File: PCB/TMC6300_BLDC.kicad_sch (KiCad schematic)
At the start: 1 part, among them U4 TMC6300-LA-T_C5274455

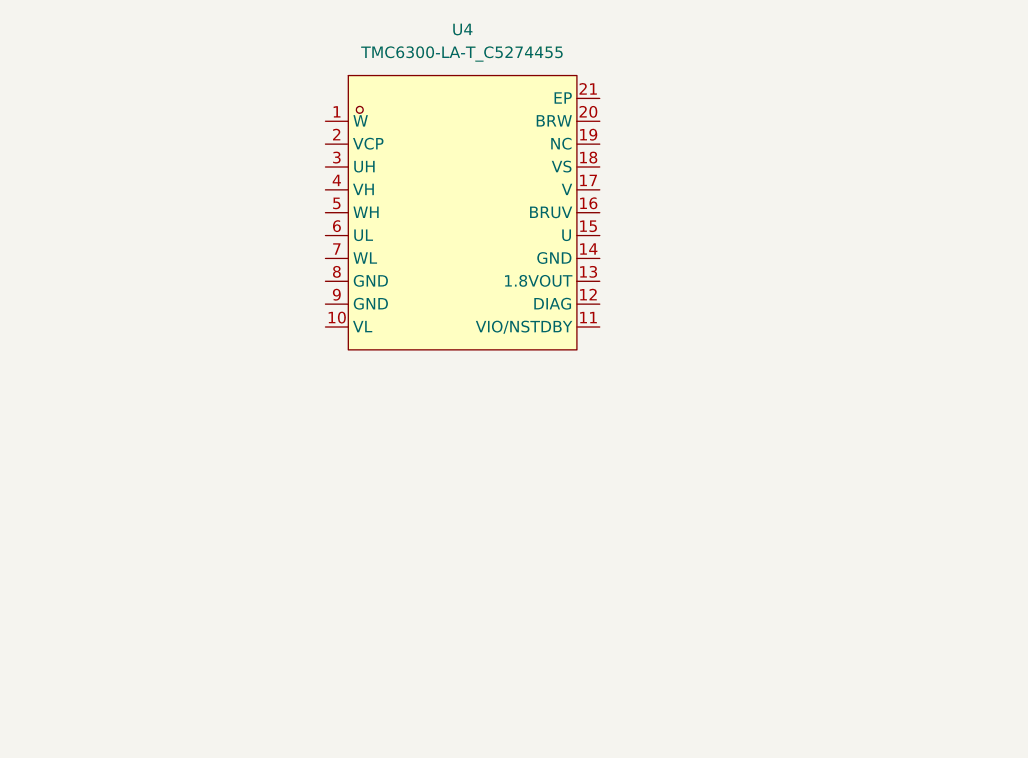
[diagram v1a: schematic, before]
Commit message: Added bldc driver
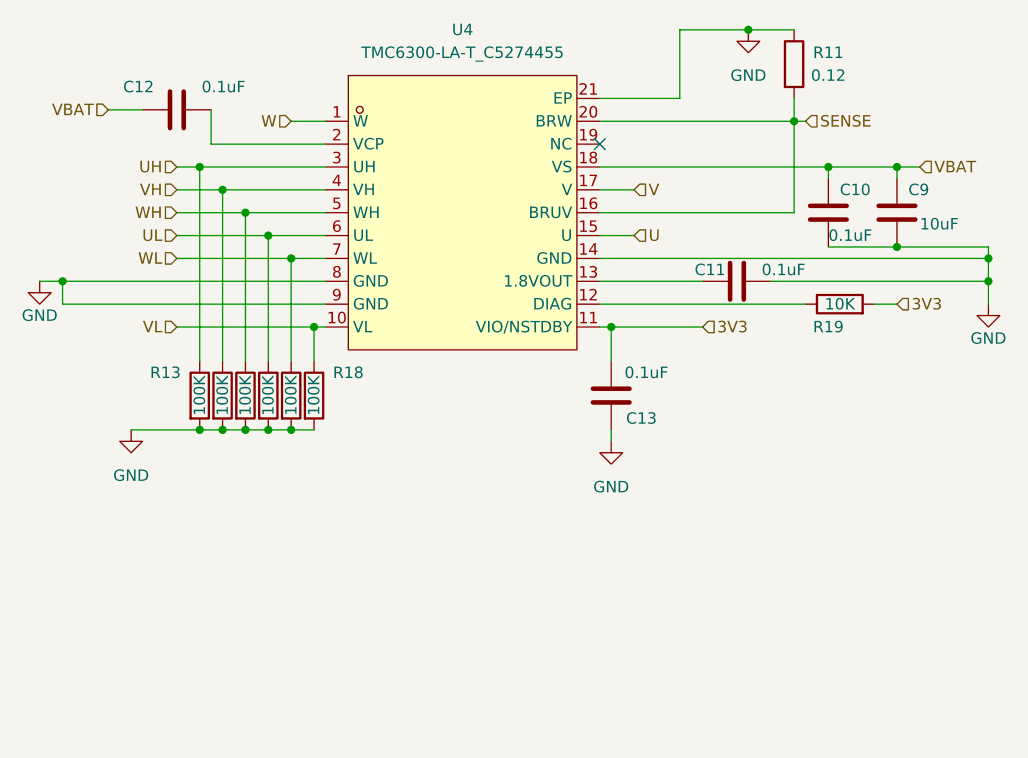
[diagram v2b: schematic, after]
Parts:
- added C10, C11, C12, C13: 0.1uF, Capacitor_SMD:C_0402_1005Metric, symbol Device:C
- added C9: 10uF, Capacitor_SMD:C_0402_1005Metric, symbol Device:C
- added R11: 0.12, Resistor_SMD:R_0402_1005Metric_Pad0.72x0.64mm_HandSolder, symbol Device:R
- added R13, R14, R15, R16, R17, R18: 100K, Resistor_SMD:R_0402_1005Metric_Pad0.72x0.64mm_HandSolder, symbol Device:R
- added R19: 10K, Resistor_SMD:R_0402_1005Metric_Pad0.72x0.64mm_HandSolder, symbol Device:R
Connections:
- net W: now reaches U4.1 (W)
- net VL: now reaches U4.10 (VL)
- net VL: now also R18.1
- net 3V3: now reaches U4.11 (VIO/NSTDBY)
- net 3V3: now also C13.2, R19.2
- net at U4.12 (DIAG): now also R19.1
- net at U4.13 (1.8VOUT): now also C11.1
- net GND: now reaches U4.14 (GND)
- net GND: now also U4.21 (EP), U4.8 (GND), U4.9 (GND), C10.2, C11.2, C13.1, C9.2, R11.1, R13.2, R14.2, R15.2, R16.2, R17.2, R18.2
- net U: now reaches U4.15 (U)
- net SENSE: now reaches U4.16 (BRUV)
- net SENSE: now also U4.20 (BRW), R11.2
- net V: now reaches U4.17 (V)
- net VBAT: now reaches U4.18 (VS)
- net VBAT: now also C10.1, C12.1, C9.1
- net at U4.2 (VCP): now also C12.2
- net UH: now reaches U4.3 (UH)
- net UH: now also R13.1
- net VH: now reaches U4.4 (VH)
- net VH: now also R14.1
- net WH: now reaches U4.5 (WH)
- net WH: now also R15.1
- net UL: now reaches U4.6 (UL)
- net UL: now also R16.1
- net WL: now reaches U4.7 (WL)
- net WL: now also R17.1
- no-connect marks 0 -> 1

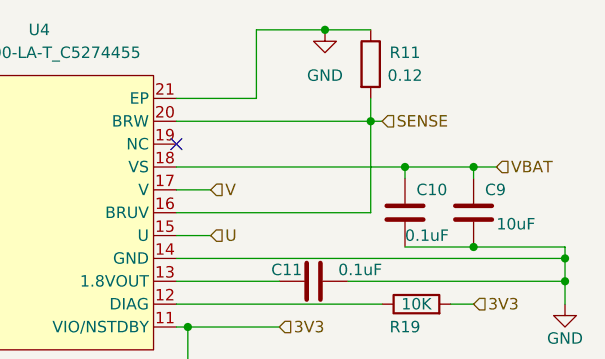
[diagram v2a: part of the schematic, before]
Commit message: BLDC driver done
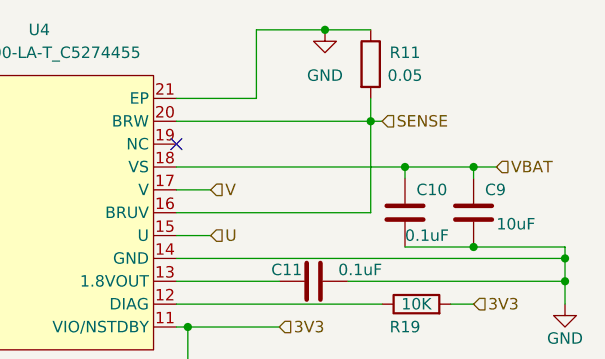
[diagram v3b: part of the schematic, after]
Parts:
- R11: value 0.12 -> 0.05; footprint Resistor_SMD:R_0402_1005Metric_Pad0.72x0.64mm_HandSolder -> Resistor_SMD:R_2010_5025Metric_Pad1.40x2.65mm_HandSolder
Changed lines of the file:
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@@
 			)
 		)
-		(property "Value" "0.12"
+		(property "Value" "0.05"
 			(at 173.99 87.63 0)
 			(effects
@@
 			)
 		)
-		(property "Footprint" "Resistor_SMD:R_0402_1005Metric_Pad0.72x0.64mm_HandSolder"
+		(property "Footprint" "Resistor_SMD:R_2010_5025Metric_Pad1.40x2.65mm_HandSolder"
 			(at 168.402 86.36 90)
 			(effects

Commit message: Finished schematic
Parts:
- C10, C12: value 0.1uF -> 0.1uF 10V
- C13: value 0.1uF -> 0.1uF 6.3V
- C9: value 10uF -> 10uF 10V
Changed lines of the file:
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@@
 			)
 		)
-		(property "Value" "0.1uF"
-			(at 156.21 120.65 0)
+		(property "Value" "0.1uF 6.3V"
+			(at 154.432 120.65 0)
 			(effects
 				(font
@@
 		(dnp no)
 		(property "Reference" "C12"
-			(at 99.06 88.9 90)
+			(at 100.076 89.916 90)
 			(effects
 				(font
@@
 			)
 		)
-		(property "Value" "0.1uF"
-			(at 109.22 88.9 90)
+		(property "Value" "0.1uF 10V"
+			(at 103.632 94.996 90)
 			(effects
 				(font
@@
 			)
 		)
-		(property "Value" "10uF"
-			(at 184.15 104.14 0)
+		(property "Value" "10uF 10V"
+			(at 182.372 105.41 0)
 			(effects
 				(font
@@
 			)
 		)
-		(property "Value" "0.1uF"
-			(at 173.99 105.41 0)
-			(effects
-				(font
+		(property "Value" "0.1uF 10V"
+			(at 168.402 105.41 0)
+			(effects
+				(font

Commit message: PCB layout done
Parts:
- removed R11: 0.05, Resistor_SMD:R_2010_5025Metric_Pad1.40x2.65mm_HandSolder, symbol Device:R
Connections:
- net SENSE is gone; now on net GND: U4.16 (BRUV), U4.20 (BRW)
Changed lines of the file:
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@@
-	)
-	(junction
-		(at 170.18 92.71)
-		(diameter 0)
-		(color 0 0 0 0)
-	)
-	(junction
-		(at 165.1 82.55)
-		(diameter 0)
-		(color 0 0 0 0)
 	)
 	(junction
@@
 	)
 	(junction
+		(at 153.67 90.17)
+		(diameter 0)
+		(color 0 0 0 0)
+	)
+	(junction
 		(at 191.77 110.49)
 		(diameter 0)
@@
 	(wire
 		(pts
+			(xy 153.67 92.71) (xy 153.67 90.17)
+		)
+		(stroke
+			(width 0)
+			(type default)
+		)
+	)
+	(wire
+		(pts
 			(xy 181.61 97.79) (xy 184.15 97.79)
 		)
@@
 	(wire
 		(pts
-			(xy 148.59 90.17) (xy 157.48 90.17)
+			(xy 148.59 90.17) (xy 153.67 90.17)
 		)
 		(stroke
@@
 	(wire
 		(pts
+			(xy 153.67 90.17) (xy 163.83 90.17)
+		)
+		(stroke
+			(width 0)
+			(type default)
+		)
+	)
+	(wire
+		(pts
 			(xy 116.84 115.57) (xy 116.84 119.38)
 		)
@@
 	(wire
 		(pts
-			(xy 157.48 90.17) (xy 157.48 82.55)
-		)
-		(stroke
-			(width 0)
-			(type default)
-		)
-	)
-	(wire
-		(pts
 			(xy 106.68 100.33) (xy 118.11 100.33)
 		)
@@
 	(wire
 		(pts
-			(xy 148.59 102.87) (xy 170.18 102.87)
-		)
-		(stroke
-			(width 0)
-			(type default)
-		)
-	)
-	(wire
-		(pts
 			(xy 109.22 127) (xy 111.76 127)
 		)
@@
 	(wire
 		(pts
-			(xy 170.18 90.17) (xy 170.18 92.71)
-		)
-		(stroke
-			(width 0)
-			(type default)
-		)
-	)
-	(wire
-		(pts
 			(xy 149.86 115.57) (xy 149.86 119.38)
 		)
@@
 	(wire
 		(pts
-			(xy 170.18 102.87) (xy 170.18 92.71)
-		)
-		(stroke
-			(width 0)
-			(type default)
-		)
-	)
-	(wire
-		(pts
 			(xy 101.6 102.87) (xy 109.22 102.87)
 		)
@@
 	(wire
 		(pts
-			(xy 165.1 82.55) (xy 170.18 82.55)
-		)
-		(stroke
-			(width 0)
-			(type default)
-		)
-	)
-	(wire
-		(pts
 			(xy 191.77 107.95) (xy 191.77 110.49)
 		)
@@
 	(wire
 		(pts
+			(xy 148.59 92.71) (xy 153.67 92.71)
+		)
+		(stroke
+			(width 0)
+			(type default)
+		)
+	)
+	(wire
+		(pts
 			(xy 111.76 105.41) (xy 118.11 105.41)
 		)
@@
 	(wire
 		(pts
-			(xy 148.59 92.71) (xy 170.18 92.71)
+			(xy 148.59 102.87) (xy 158.75 102.87)
 		)
 		(stroke
@@
 	(wire
 		(pts
-			(xy 157.48 82.55) (xy 165.1 82.55)
-		)
-		(stroke
-			(width 0)
-			(type default)
-		)
-	)
-	(wire
-		(pts
 			(xy 148.59 97.79) (xy 173.99 97.79)
 		)
@@
 		(pts
 			(xy 101.6 105.41) (xy 111.76 105.41)
-		)
-		(stroke
-			(width 0)
-			(type default)
-		)
-	)
-	(wire
-		(pts
-			(xy 170.18 92.71) (xy 171.45 92.71)
 		)
 		(stroke
@@
 			)
 			(justify right)
-		)
-	)
-	(hierarchical_label "SENSE"
-		(shape input)
-		(at 171.45 92.71 0)
-		(effects
-			(font
-				(size 1.27 1.27)
-			)
-			(justify left)
 		)
 	)
@@
 	)
 	(symbol
+		(lib_id "power:GND")
+		(at 163.83 90.17 0)
+		(unit 1)
+		(exclude_from_sim no)
+		(in_bom yes)
+		(on_board yes)
+		(dnp no)
+		(fields_autoplaced yes)
+		(property "Reference" "#PWR059"
+			(at 163.83 96.52 0)
+			(effects
+				(font
+					(size 1.27 1.27)
+				)
+				(hide yes)
+			)
+		)
+		(property "Value" "GND"
+			(at 163.83 95.25 0)
+			(effects
+				(font
+					(size 1.27 1.27)
+				)
+			)
+		)
+		(property "Footprint" ""
+			(at 163.83 90.17 0)
+			(effects
+				(font
+					(size 1.27 1.27)
+				)
+				(hide yes)
+			)
+		)
+		(property "Datasheet" ""
+			(at 163.83 90.17 0)
+			(effects
+				(font
+					(size 1.27 1.27)
+				)
+				(hide yes)
+			)
+		)
+		(property "Description" "Power symbol creates a global label with name \"GND\" , ground"
+			(at 163.83 90.17 0)
+			(effects
+				(font
+					(size 1.27 1.27)
+				)
+				(hide yes)
+			)
+		)
+		(pin "1"
+		)
+		(instances
+			(project ""
+				(path "/64c66767-4367-4391-b4db-5d3ae338f23b/f7d2473e-319a-4a76-8dbf-73a91e1f555e"
+					(reference "#PWR059")
+					(unit 1)
+				)
+			)
+		)
+	)
+	(symbol
 		(lib_id "Device:R")
 		(at 114.3 123.19 0)
@@
 				(path "/64c66767-4367-4391-b4db-5d3ae338f23b/f7d2473e-319a-4a76-8dbf-73a91e1f555e"
 					(reference "R13")
-					(unit 1)
-				)
-			)
-		)
-	)
-	(symbol
-		(lib_id "power:GND")
-		(at 165.1 82.55 0)
-		(unit 1)
-		(exclude_from_sim no)
-		(in_bom yes)
-		(on_board yes)
-		(dnp no)
-		(fields_autoplaced yes)
-		(property "Reference" "#PWR018"
-			(at 165.1 88.9 0)
-			(effects
-				(font
-					(size 1.27 1.27)
-				)
-				(hide yes)
-			)
-		)
-		(property "Value" "GND"
-			(at 165.1 87.63 0)
-			(effects
-				(font
-					(size 1.27 1.27)
-				)
-			)
-		)
-		(property "Footprint" ""
-			(at 165.1 82.55 0)
-			(effects
-				(font
-					(size 1.27 1.27)
-				)
-				(hide yes)
-			)
-		)
-		(property "Datasheet" ""
-			(at 165.1 82.55 0)
-			(effects
-				(font
-					(size 1.27 1.27)
-				)
-				(hide yes)
-			)
-		)
-		(property "Description" "Power symbol creates a global label with name \"GND\" , ground"
-			(at 165.1 82.55 0)
-			(effects
-				(font
-					(size 1.27 1.27)
-				)
-				(hide yes)
-			)
-		)
-		(pin "1"
-		)
-		(instances
-			(project ""
-				(path "/64c66767-4367-4391-b4db-5d3ae338f23b/f7d2473e-319a-4a76-8dbf-73a91e1f555e"
-					(reference "#PWR018")
 					(unit 1)
 				)
@@
 	(symbol
 		(lib_id "Device:R")
-		(at 170.18 86.36 0)
-		(unit 1)
-		(exclude_from_sim no)
-		(in_bom yes)
-		(on_board yes)
-		(dnp no)
-		(property "Reference" "R11"
-			(at 173.99 85.09 0)
-			(effects
-				(font
-					(size 1.27 1.27)
-				)
-			)
-		)
-		(property "Value" "0.05"
-			(at 173.99 87.63 0)
-			(effects
-				(font
-					(size 1.27 1.27)
-				)
-			)
-		)
-		(property "Footprint" "Resistor_SMD:R_2010_5025Metric_Pad1.40x2.65mm_HandSolder"
-			(at 168.402 86.36 90)
-			(effects
-				(font
-					(size 1.27 1.27)
-				)
-				(hide yes)
-			)
-		)
-		(property "Datasheet" "~"
-			(at 170.18 86.36 0)
-			(effects
-				(font
-					(size 1.27 1.27)
-				)
-				(hide yes)
-			)
-		)
-		(property "Description" "Resistor"
-			(at 170.18 86.36 0)
-			(effects
-				(font
-					(size 1.27 1.27)
-				)
-				(hide yes)
-			)
-		)
-		(pin "1"
-		)
-		(pin "2"
-		)
-		(instances
-			(project "detentOne"
-				(path "/64c66767-4367-4391-b4db-5d3ae338f23b/f7d2473e-319a-4a76-8dbf-73a91e1f555e"
-					(reference "R11")
-					(unit 1)
-				)
-			)
-		)
-	)
-	(symbol
-		(lib_id "Device:R")
 		(at 116.84 123.19 0)
 		(unit 1)
@@
 					(unit 1)
 				)
+			)
+		)
+	)
+	(symbol
+		(lib_id "power:GND")
+		(at 158.75 102.87 0)
+		(unit 1)
+		(exclude_from_sim no)
+		(in_bom yes)
+		(on_board yes)
+		(dnp no)
+		(property "Reference" "#PWR018"
+			(at 158.75 109.22 0)
+			(effects
+				(font
+					(size 1.27 1.27)
+				)
+				(hide yes)
+			)
+		)
+		(property "Value" "GND"
+			(at 161.036 106.172 0)
+			(effects
+				(font
+					(size 1.27 1.27)
+				)
+			)
+		)
+		(property "Footprint" ""
+			(at 158.75 102.87 0)
+			(effects
+				(font
+					(size 1.27 1.27)
+				)
+				(hide yes)
+			)
+		)
+		(property "Datasheet" ""
+			(at 158.75 102.87 0)
+			(effects
+				(font
+					(size 1.27 1.27)
+				)
+				(hide yes)
+			)
+		)
+		(property "Description" "Power symbol creates a global label with name \"GND\" , ground"
+			(at 158.75 102.87 0)
+			(effects
+				(font
+					(size 1.27 1.27)
+				)
+				(hide yes)
+			)
+		)
+		(pin "1"
+		)
+		(instances
+			(project "detentOne"
+				(path "/64c66767-4367-4391-b4db-5d3ae338f23b/f7d2473e-319a-4a76-8dbf-73a91e1f555e"
+					(reference "#PWR018")
+					(unit 1)
+				)

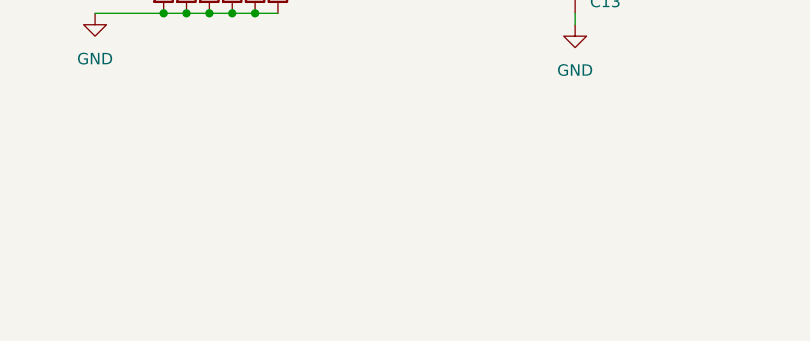
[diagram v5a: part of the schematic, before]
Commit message: removed lipo circuitry
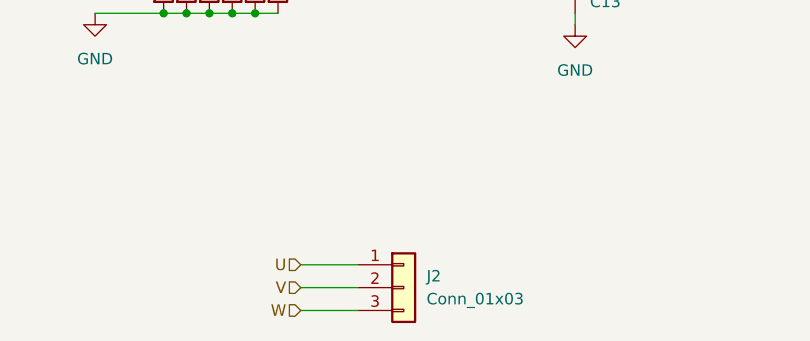
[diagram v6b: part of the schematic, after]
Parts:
- added J2: Conn_01x03, Connector_PinHeader_2.54mm:PinHeader_1x03_P2.54mm_Horizontal, symbol Connector_Generic:Conn_01x03
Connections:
- net U: now also J2.1 (Pin_1)
- net V: now also J2.2 (Pin_2)
- net W: now also J2.3 (Pin_3)
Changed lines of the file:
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@@
+	(wire
+		(pts
+			(xy 119.38 154.94) (xy 125.73 154.94)
+		)
+		(stroke
+			(width 0)
+			(type default)
+		)
+	)
 	(wire
 		(pts
@@
 	(wire
 		(pts
+			(xy 119.38 160.02) (xy 125.73 160.02)
+		)
+		(stroke
+			(width 0)
+			(type default)
+		)
+	)
+	(wire
+		(pts
 			(xy 109.22 102.87) (xy 118.11 102.87)
 		)
@@
 		(pts
 			(xy 173.99 97.79) (xy 181.61 97.79)
+		)
+		(stroke
+			(width 0)
+			(type default)
+		)
+	)
+	(wire
+		(pts
+			(xy 119.38 157.48) (xy 125.73 157.48)
 		)
 		(stroke
@@
 		)
 	)
+	(hierarchical_label "V"
+		(shape input)
+		(at 119.38 157.48 180)
+		(effects
+			(font
+				(size 1.27 1.27)
+			)
+			(justify right)
+		)
+	)
 	(hierarchical_label "W"
 		(shape input)
@@
 		)
 	)
+	(hierarchical_label "W"
+		(shape input)
+		(at 119.38 160.02 180)
+		(effects
+			(font
+				(size 1.27 1.27)
+			)
+			(justify right)
+		)
+	)
 	(hierarchical_label "VBAT"
 		(shape input)
@@
 			)
 			(justify left)
+		)
+	)
+	(hierarchical_label "U"
+		(shape input)
+		(at 119.38 154.94 180)
+		(effects
+			(font
+				(size 1.27 1.27)
+			)
+			(justify right)
 		)
 	)
@@
 					(unit 1)
 				)
+			)
+		)
+	)
+	(symbol
+		(lib_id "Connector_Generic:Conn_01x03")
+		(at 130.81 157.48 0)
+		(unit 1)
+		(exclude_from_sim no)
+		(in_bom yes)
+		(on_board yes)
+		(dnp no)
+		(fields_autoplaced yes)
+		(property "Reference" "J2"
+			(at 133.35 156.2099 0)
+			(effects
+				(font
+					(size 1.27 1.27)
+				)
+				(justify left)
+			)
+		)
+		(property "Value" "Conn_01x03"
+			(at 133.35 158.7499 0)
+			(effects
+				(font
+					(size 1.27 1.27)
+				)
+				(justify left)
+			)
+		)
+		(property "Footprint" "Connector_PinHeader_2.54mm:PinHeader_1x03_P2.54mm_Horizontal"
+			(at 130.81 157.48 0)
+			(effects
+				(font
+					(size 1.27 1.27)
+				)
+				(hide yes)
+			)
+		)
+		(property "Datasheet" "~"
+			(at 130.81 157.48 0)
+			(effects
+				(font
+					(size 1.27 1.27)
+				)
+				(hide yes)
+			)
+		)
+		(property "Description" "Generic connector, single row, 01x03, script generated (kicad-library-utils/schlib/autogen/connector/)"
+			(at 130.81 157.48 0)
+			(effects
+				(font
+					(size 1.27 1.27)
+				)
+				(hide yes)
+			)
+		)
+		(pin "2"
+		)
+		(pin "3"
+		)
+		(pin "1"
+		)
+		(instances
+			(project ""
+				(path "/64c66767-4367-4391-b4db-5d3ae338f23b/f7d2473e-319a-4a76-8dbf-73a91e1f555e"
+					(reference "J2")
+					(unit 1)
+				)
